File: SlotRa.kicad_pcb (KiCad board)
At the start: 2 copper layers, 25.4 x 52.1 mm, 36 parts, among them J1 Nice!nano - left pins, J10 Battery Holes, J14 GPS Pins, J2 Nice!nano - right pins, J3 Lora - left pins, J4 Lora - right pins, J5 I2C Oled screen, J6 T1 Drain - SMD, J7 T2 Drain - SMD, J8 T3 Drain - SMD, J9 Battery Connector JST 1.25, SW1 Reset, SW2 SW_Push, T1 SI2312, T2 SI2312, T3 SI2312, U1 XB8089D0

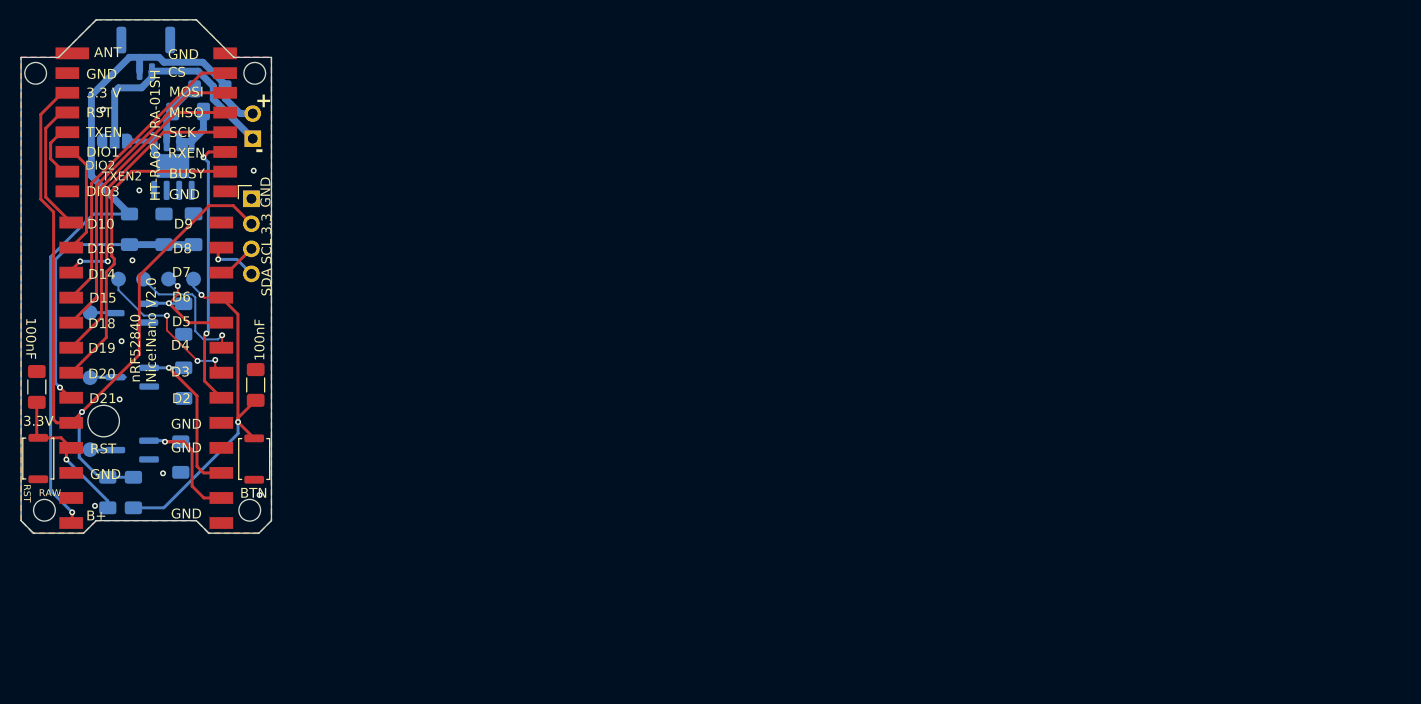
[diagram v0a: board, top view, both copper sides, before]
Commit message: Finally, The PCB
Small fixes in the schematics.
Recreated the PCB. A toucght one, there were too many wrong decisions that led to a non-upgradability of the project without the Power Of Some Mother And The Sledgehammer.
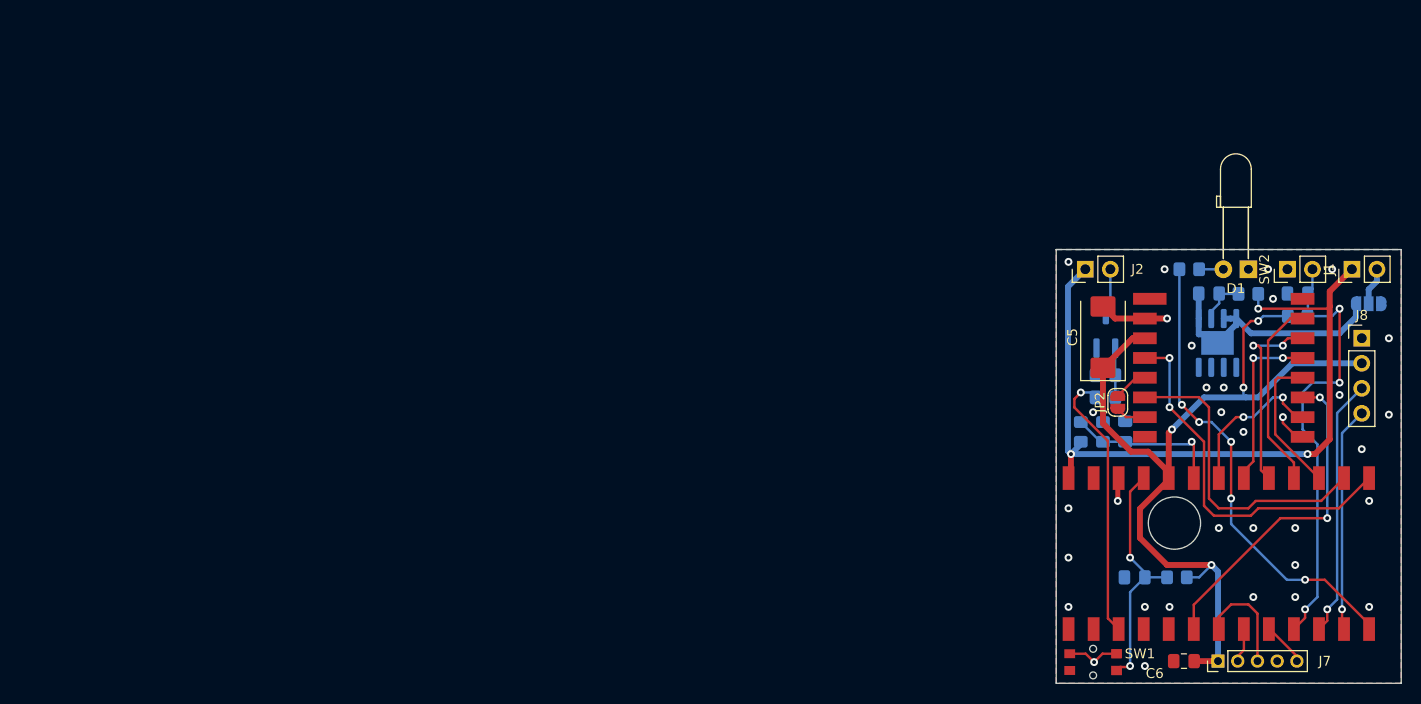
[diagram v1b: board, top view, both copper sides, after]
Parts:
- removed ? (x3): , 
- removed G***: LOGO, SMD_PAD:Shimon_kicad
- removed J14: GPS Pins, SMD_PAD:SMD_PAD_4x1
- removed the J7 at (98.0, 123.5)
- removed the J8 at (98.0, 130.8)
- removed the R1 at (107.5, 117.5)
- removed the R3 at (107.2, 131.6)
- removed the REF** at (99.4, 127.9)
- removed the REF** at (114.7, 92.6)
- removed T2, T3: SI2312, SMD_PAD:TSOT-23_HandSoldering_Updated
- added C5: 100u 6.3V, Capacitor_Tantalum_SMD:CP_EIA-7343-31_Kemet-D, F.Cu at (200.8, 119.4)
- added C6: 100nF, Capacitor_SMD:C_0805_2012Metric_Pad1.18x1.45mm_HandSolder, F.Cu at (209.0, 152.2)
- added D1: LED_White, LED_THT:LED_D3.0mm_Horizontal_O6.35mm_Z10.0mm, F.Cu at (215.5, 112.5)
- added JP2: JP-TX-DIO2, Jumper:SolderJumper-2_P1.3mm_Open_RoundedPad1.0x1.5mm, F.Cu at (202.2, 126.0)
- added R6: 270, Resistor_SMD:R_0805_2012Metric_Pad1.20x1.40mm_HandSolder, B.Cu at (209.5, 112.5)
- added R7: 100, Resistor_SMD:R_0805_2012Metric_Pad1.20x1.40mm_HandSolder, B.Cu at (201.0, 125.5)
- added REF**: MountingHole_5.3mm_M5, SlotRa:MountingHole_5.3mm_M5, F.Cu at (208.0, 138.2)
- C1: renamed from C3; footprint Capacitor_SMD:C_1206_3216Metric_Pad1.33x1.80mm_HandSolder -> Capacitor_SMD:C_0805_2012Metric_Pad1.18x1.45mm_HandSolder; moved to B.Cu
- C2: renamed from C1; footprint Capacitor_SMD:C_1206_3216Metric_Pad1.33x1.80mm_HandSolder -> Capacitor_SMD:C_0805_2012Metric_Pad1.18x1.45mm_HandSolder
- C3: renamed from C2; footprint Capacitor_SMD:C_1206_3216Metric_Pad1.33x1.80mm_HandSolder -> Capacitor_SMD:C_0805_2012Metric_Pad1.18x1.45mm_HandSolder
- C4: footprint Capacitor_SMD:C_1206_3216Metric_Pad1.33x1.80mm_HandSolder -> Capacitor_SMD:C_0805_2012Metric_Pad1.18x1.45mm_HandSolder; moved to B.Cu
- J1: renamed from J10; value Battery Holes -> PinsBatt; moved to F.Cu
- J2: renamed from J6; value T1 Drain - SMD -> Conn_Out_Ext; footprint SMD_PAD:SMD_PAD_1x1 -> Connector_PinHeader_2.54mm:PinHeader_1x02_P2.54mm_Vertical; moved to F.Cu
- J3: renamed from J1; value Nice!nano - left pins -> ControllerL; footprint SMD_PAD:SMD_Pad_Row_P2.54_13x1 -> SlotRa:SMD_Pad_Row_P2.54_13x1
- J4: renamed from J3; value Lora - left pins -> ModemL; footprint SMD_PAD:SMD_Pad_Row_P2.00_8x1_longer -> SlotRa:SMD_Pad_Row_P2.00_8x1_longer
- J5: renamed from J2; value Nice!nano - right pins -> ControllerR; footprint SMD_PAD:SMD_Pad_Row_P2.54_13x1 -> SlotRa:SMD_Pad_Row_P2.54_13x1
- J6: renamed from J4; value Lora - right pins -> ModemR; footprint SMD_PAD:SMD_Pad_Row_P2.00_8x1 -> SlotRa:SMD_Pad_Row_P2.00_8x1
- J7: renamed from J9; value Battery Connector JST 1.25 -> Conn_GPS; footprint Connector_JST:JST_GH_SM02B-GHS-TB_1x02-1MP_P1.25mm_Horizontal -> Connector_PinHeader_2.00mm:PinHeader_1x05_P2.00mm_Vertical; moved to F.Cu
- J8: renamed from J5; value I2C Oled screen -> Conn_I2C
- JP1: value Jumper_3_Open -> JP-EnableProt
- R1: renamed from R4; value 10M -> 1M; footprint Resistor_SMD:R_1206_3216Metric_Pad1.30x1.75mm_HandSolder -> Resistor_SMD:R_0805_2012Metric_Pad1.20x1.40mm_HandSolder
- R2: renamed from R8; footprint Resistor_SMD:R_1206_3216Metric_Pad1.30x1.75mm_HandSolder -> Resistor_SMD:R_0805_2012Metric_Pad1.20x1.40mm_HandSolder
- R3: renamed from R5; value 10M -> 1.5M; footprint Resistor_SMD:R_1206_3216Metric_Pad1.30x1.75mm_HandSolder -> Resistor_SMD:R_0805_2012Metric_Pad1.20x1.40mm_HandSolder
- R4: renamed from R7; footprint Resistor_SMD:R_1206_3216Metric_Pad1.30x1.75mm_HandSolder -> Resistor_SMD:R_0805_2012Metric_Pad1.20x1.40mm_HandSolder
- R5: renamed from R6; footprint Resistor_SMD:R_1206_3216Metric_Pad1.30x1.75mm_HandSolder -> Resistor_SMD:R_0805_2012Metric_Pad1.20x1.40mm_HandSolder
- R8: renamed from R2; footprint Resistor_SMD:R_1206_3216Metric_Pad1.30x1.75mm_HandSolder -> Resistor_SMD:R_0805_2012Metric_Pad1.20x1.40mm_HandSolder
- SW1: value Reset -> ButRst; footprint Button_Switch_SMD:SW_Push_SPST_NO_Alps_SKRK -> SlotRa:KLS7-TS6335
- SW2: value SW_Push -> ButUsr; footprint Button_Switch_SMD:SW_Push_SPST_NO_Alps_SKRK -> Connector_PinHeader_2.54mm:PinHeader_1x02_P2.54mm_Vertical
- T1: footprint SMD_PAD:TSOT-23_HandSoldering_Updated -> SlotRa:TSOT-23_HandSoldering_Updated
- moved J3 134.2 mm to (227.7, 133.7), turned to -90 degrees
- moved JP1 128.3 mm to (227.7, 116.0), turned to 0 degrees
- moved J7 125.0 mm to (212.4, 152.2), turned to 90 degrees
- moved J5 123.5 mm to (227.7, 149.0), turned to -90 degrees
- moved R4 119.4 mm to (220.5, 117.2), turned to 180 degrees
- moved J8 113.5 mm to (227.0, 119.5)
- moved C1 113.0 mm to (204.0, 143.8), turned to 180 degrees
- moved J1 112.3 mm to (226.0, 112.5), turned to 90 degrees
- moved J4 112.1 mm to (205.0, 115.5)
- moved J6 112.1 mm to (221.0, 115.5)
- moved SW1 109.0 mm to (199.8, 152.3), turned to 0 degrees
- moved R2 108.8 mm to (208.2, 143.8), turned to 180 degrees
- moved U1 107.5 mm to (212.4, 120.0)
- moved R5 107.4 mm to (215.5, 115.0)
- moved SW2 106.6 mm to (219.5, 112.5)
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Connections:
- net /BTN renamed /BTN_USR
- net /RST_BTN renamed /BTN_RST
- C2 pad 1: /Batt% -> /ADC_BATT
- J1 pad 1: -BATT -> +BATT
- J1 pad 2: +BATT -> -BATT
- J2 pad 1: Net-(J6-Pin_1) -> +BATT
- J3 pad 8: /Batt% -> /ADC_BATT
- J4 pad 5: Net-(J3-Pin_5) -> /TXEN
- J4 pad 7: Net-(J3-Pin_5) -> /DIO2
- J5 pad 1: unconnected-(J2-Pin_1-Pad1) -> /LED_USR
- J5 pad 10: unconnected-(J2-Pin_10-Pad10) -> GND
- J5 pad 11: /T2G -> /OUT_EXT
- J5 pad 12: /T3G -> unconnected-(J5-Pin_12-Pad12)
- J5 pad 5: /T1G -> /GPS_EN
- J5 pad 6: Net-(J14-Pin_3) -> /GPS_TX
- J5 pad 7: Net-(J14-Pin_4) -> /GPS_RX
- J5 pad 9: unconnected-(J2-Pin_9-Pad9) -> GND
- J7 pad 1: +BATT -> +3.3V
- J7 pad 2: -BATT -> /GPS_TX
- R1 pad 1: /Batt% -> +BATT
- R1 pad 2: +BATT -> /ADC_BATT
- R3 pad 1: /Batt% -> /ADC_BATT
- R8 pad 2: /T2G -> Net-(T1-G)
- T1 pad 1: Net-(J6-Pin_1) -> Net-(J2-Pin_2)
- T1 pad 2: /T1G -> Net-(T1-G)
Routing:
- net /LED_USR: track 0.00 -> 47.5 mm, vias 0 -> 5
- net /Batt%: track 29.4 -> 0.00 mm, vias 1 -> 0
- net /OUT_EXT: track 0.00 -> 27.8 mm, vias 0 -> 1
- net /RST: track 13.5 -> 37.7 mm, vias 0 -> 2
- net /SCL: track 4.05 -> 26.2 mm, vias 0 -> 1
- net /DIO1: track 11.5 -> 31.6 mm
- net -BATT: track 23.8 -> 3.85 mm
- net GND: track 0.00 -> 18.0 mm, vias 9 -> 33
- net /SDA: track 5.31 -> 22.8 mm
- net /BUSY: track 32.7 -> 15.7 mm, vias 0 -> 2
- net /T2G: track 16.4 -> 0.00 mm, vias 1 -> 0
- net Net-(J14-Pin_4): track 16.4 -> 0.00 mm, vias 3 -> 0
- net /ADC_BATT: track 0.00 -> 16.1 mm, vias 0 -> 1
- net /MISO: track 33.2 -> 17.6 mm, vias 0 -> 2
- net Net-(JP1-A): track 11.6 -> 25.7 mm
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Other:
- board size 25.4 x 52.1 mm -> 35 x 44 mm
- board text removed: "+"
- board text removed: "-"
- board text removed: "."
- board text removed: "100nF"
- board text removed: "10M"
- board text removed: "10k"
- board text removed: "1k"
- board text removed: "3.3"
- board text removed: "3.3 V"
- board text removed: "3.3V"
- board text removed: "ANT"
- board text removed: "B+"
- board text removed: "BMS>"
- board text removed: "BTN"
- board text removed: "BUSY"
- board text removed: "CS"
- board text removed: "D"
- board text removed: "D10"
- board text removed: "D14"
- board text removed: "D15"
- board text removed: "D16"
- board text removed: "D18"
- board text removed: "D19"
- board text removed: "D2"
- board text removed: "D20"
- board text removed: "D21"
- board text removed: "D3"
- board text removed: "D4"
- board text removed: "D5"
- board text removed: "D6"
- board text removed: "D7"
- board text removed: "D8"
- board text removed: "D9"
- board text removed: "DIO1"
- board text removed: "DIO2"
- board text removed: "DIO3"
- board text removed: "EN"
- board text removed: "G"
- board text removed: "GND"
- board text removed: "GPS:"
- board text removed: "HT-RA62 / RA-01SH"
- board text removed: "JST 1,25"
- board text removed: "Li-Ion or Li-Pol battery charging done by Nice!Nano protected with XB8089D0"
- board text removed: "MISO"
- board text removed: "MOSI"
- board text removed: "OLED Screen"
- board text removed: "RAW"
- board text removed: "RST"
- board text removed: "RXEN"
- board text removed: "Resistors and capacitors are 1206"
- board text removed: "S"
- board text removed: "SCK"
- board text removed: "SCL"
- board text removed: "SDA"
- board text removed: "SI2312"
- board text removed: "T1"
- board text removed: "T2"
- board text removed: "T3"
- board text removed: "TO RX"
- board text removed: "TO TX"
- board text removed: "TXEN"
- board text removed: "TXEN2"
- board text removed: "XB8089D0"
- board text removed: "charge < boost 300 mA"
- board text removed: "direct>"
- board text removed: "fakeTec v5 Made with ♥ by Shimon"
- board text removed: "nRF52840 Nice!Nano V2.0"

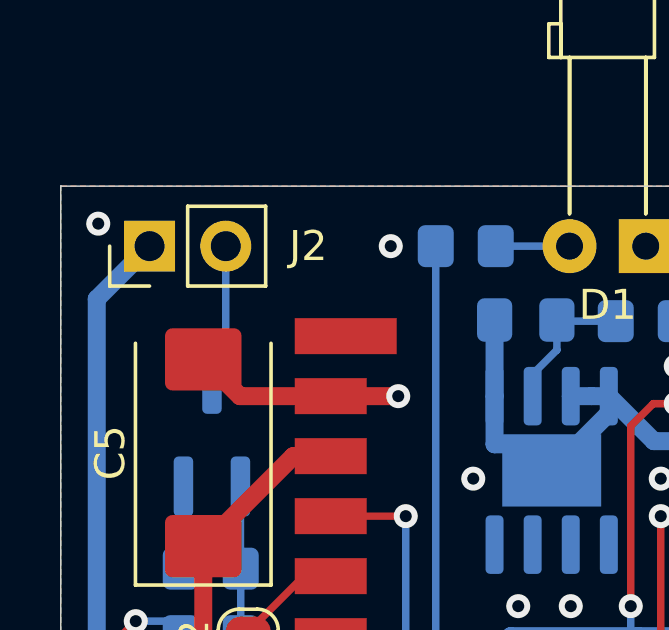
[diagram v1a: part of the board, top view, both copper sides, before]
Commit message: Quick Fix: MOSFET line
Just a quick fix: T1 Drain circuit was too thin. It's in the Power family now, so the line is thick.
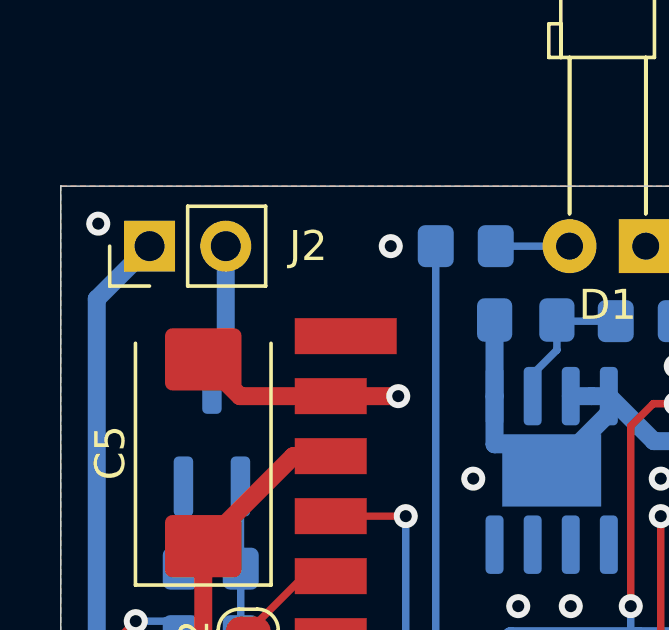
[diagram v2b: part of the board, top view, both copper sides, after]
